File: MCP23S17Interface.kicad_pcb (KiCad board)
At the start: 2 copper layers, 55.8 x 45.4 mm, 8 parts, among them J1 Conn_01x09, J2 Conn_01x16, J3 Conn_01x03, J4 Conn_01x03, J5 Conn_01x03, U1 MCP23S17_SP

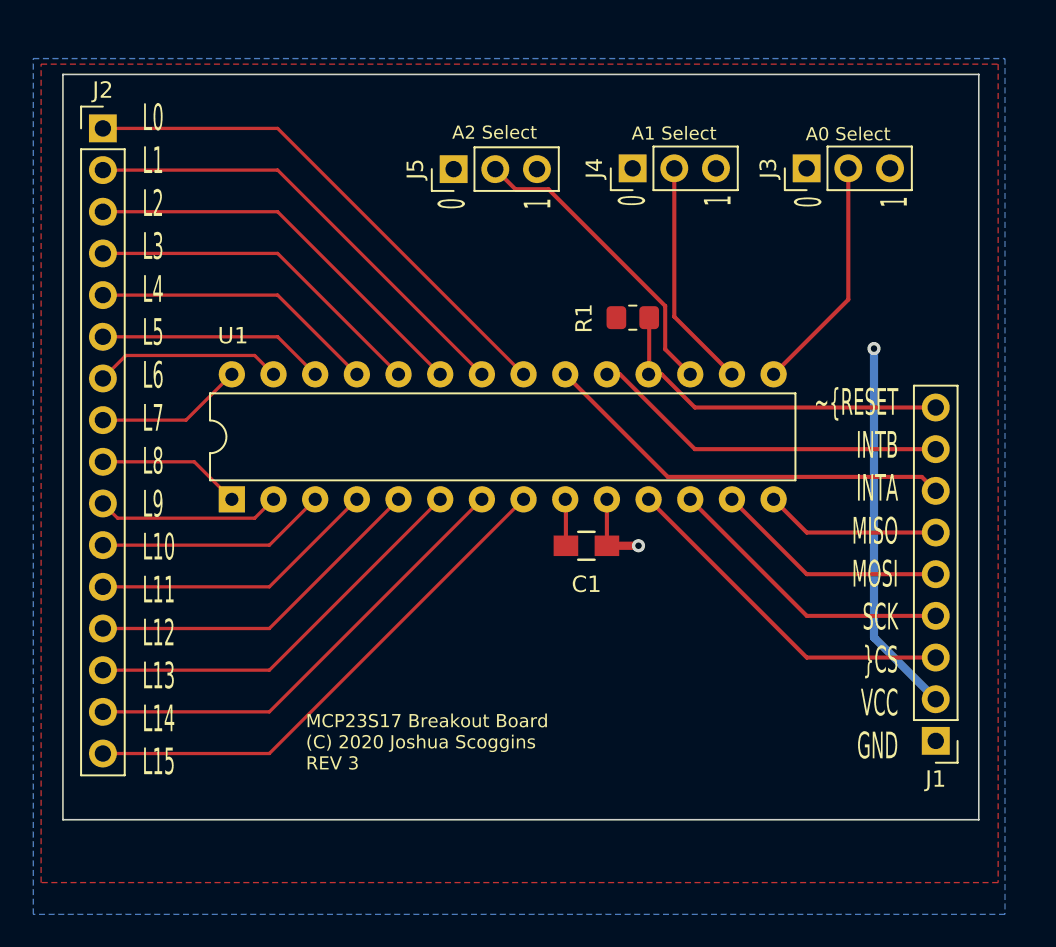
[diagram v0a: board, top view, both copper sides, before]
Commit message: Start working on the new PCB
Rearrange ordering of dip switches to make routing easier
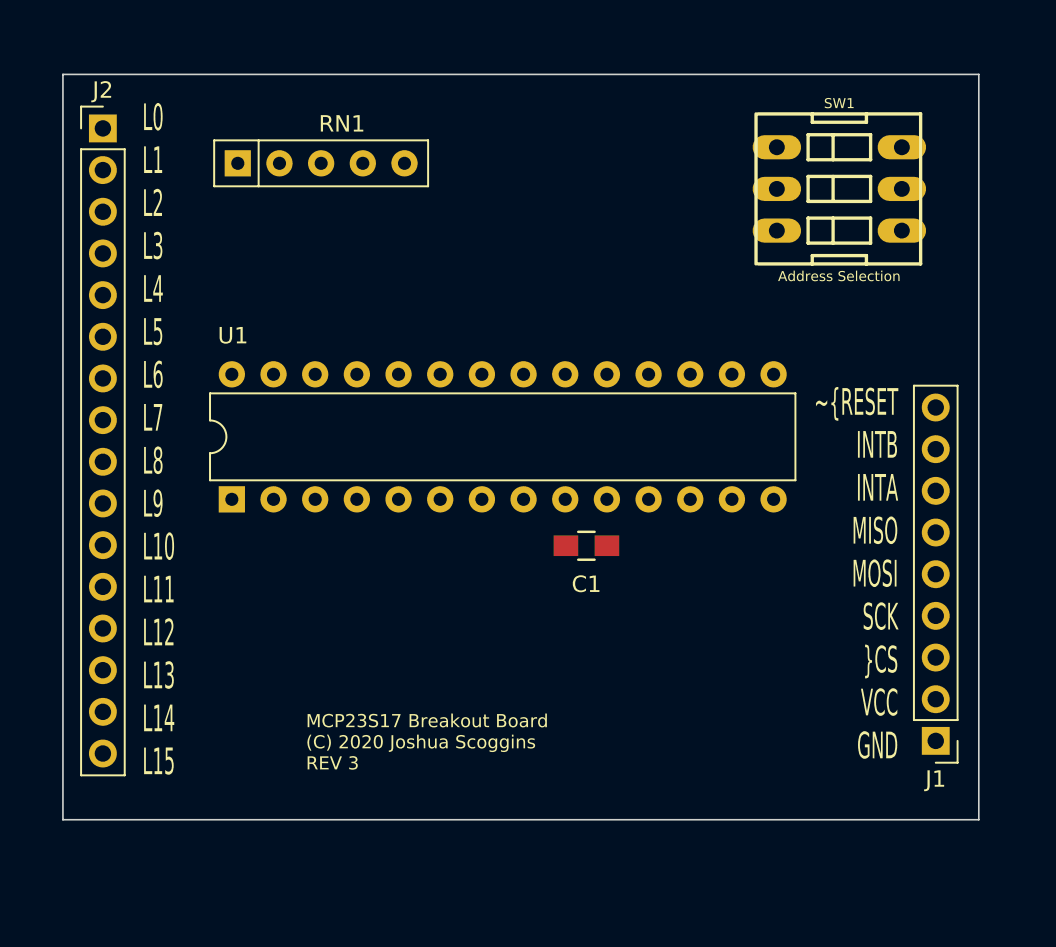
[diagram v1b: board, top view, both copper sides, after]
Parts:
- removed J3, J4, J5: Conn_01x03, Connector_PinHeader_2.54mm:PinHeader_1x03_P2.54mm_Vertical
- removed R1: 10k, Resistor_SMD:R_0805_2012Metric_Pad1.20x1.40mm_HandSolder
- added RN1: 10k, Resistor_THT:R_Array_SIP5, F.Cu at (102.7, 34.1)
- added SW1: Address Selection, Switches:DIPSWITCH-03, F.Cu at (139.3, 42.0)
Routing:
- net /L15: track 32.1 -> 0.00 mm
- net /L0: track 31.8 -> 0.00 mm
- net /L14: track 28.5 -> 0.00 mm
- net /L1: track 28.3 -> 0.00 mm
- net VCC: track 25.8 -> 0.00 mm, vias 1 -> 0
- net /INTA: track 25.5 -> 0.00 mm
- net /L13: track 24.9 -> 0.00 mm
- net /L2: track 24.7 -> 0.00 mm
- net /INTB: track 21.9 -> 0.00 mm
- net /~RESET: track 21.8 -> 0.00 mm
- net /~CS: track 21.5 -> 0.00 mm
- net /L12: track 21.3 -> 0.00 mm
- net /L3: track 21.1 -> 0.00 mm
- net /A2: track 18.6 -> 0.00 mm
- net /SCK: track 17.9 -> 0.00 mm
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- removed copper zone on B.Cu, net GND
- removed copper zone on F.Cu, net VCC
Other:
- board text removed: "0 1"
- board text removed: "A0 Select"
- board text removed: "A1 Select"
- board text removed: "A2 Select"

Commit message: Finished the rev 4 design
I have routed the resistor network directly into the trace but I'm not
sure if that is the smarter design or not. I will ponder further on this
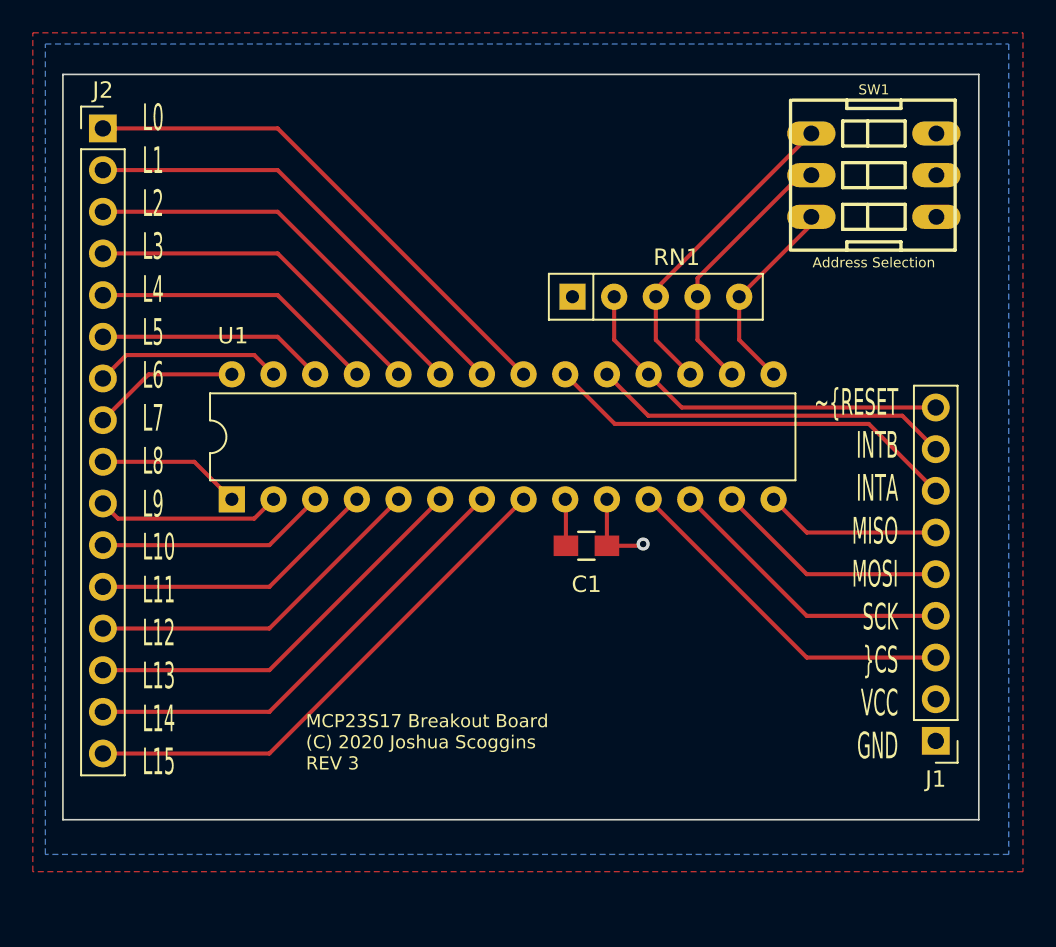
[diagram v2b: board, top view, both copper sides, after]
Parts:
- moved RN1 22.0 mm to (123.1, 42.2)
- moved SW1 2.26 mm to (141.4, 41.1)
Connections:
- RN1 pad 3: /A0 -> /A2
- RN1 pad 5: /A2 -> /A0
- SW1 pad 1: /A0 -> /A2
- SW1 pad 3: /A2 -> /A0
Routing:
- net /L15: track 0.00 -> 32.1 mm
- net /L0: track 0.00 -> 31.8 mm
- net /L14: track 0.00 -> 28.5 mm
- net /L1: track 0.00 -> 28.3 mm
- net /INTA: track 0.00 -> 25.5 mm
- net /L13: track 0.00 -> 24.9 mm
- net /L2: track 0.00 -> 24.7 mm
- net /~RESET: track 0.00 -> 23.9 mm
- net /INTB: track 0.00 -> 21.9 mm
- net /~CS: track 0.00 -> 21.5 mm
- net /L12: track 0.00 -> 21.3 mm
- net /L3: track 0.00 -> 21.1 mm
- net /A2: track 0.00 -> 19.5 mm
- net /SCK: track 0.00 -> 17.9 mm
- net /L11: track 0.00 -> 17.7 mm
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- added copper zone on B.Cu, net GND
- added copper zone on F.Cu, net VCC

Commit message: Rearrange lines further to reduce trace fanout
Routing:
- net /L15: track 32.1 -> 0.00 mm
- net /L0: track 31.8 -> 0.00 mm
- net /L14: track 28.5 -> 0.00 mm
- net /L1: track 28.3 -> 0.00 mm
- net /INTA: track 25.5 -> 0.00 mm
- net /L13: track 24.9 -> 0.00 mm
- net /L2: track 24.7 -> 0.00 mm
- net /~RESET: track 23.9 -> 0.00 mm
- net /INTB: track 21.9 -> 0.00 mm
- net /~CS: track 21.5 -> 0.00 mm
- net /L12: track 21.3 -> 0.00 mm
- net /L3: track 21.1 -> 0.00 mm
- net /A2: track 19.5 -> 0.00 mm
- net /SCK: track 17.9 -> 0.00 mm
- net /L11: track 17.7 -> 0.00 mm
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- removed copper zone on B.Cu, net GND
- removed copper zone on F.Cu, net VCC
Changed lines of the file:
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@@
     (thickness 1.6002)
     (drawings 7)
-    (tracks 72)
+    (tracks 0)
     (zones 0)
     (modules 6)
@@
     (effects (font (size 1.6256 0.8) (thickness 0.1)) (justify right))
   )
-  (via (at 127.36576 57.26938) (size 0.8) (drill 0.4) (layers Front Back) (net 1))
-  (segment (start 125.15628 57.37606) (end 127.25908 57.37606) (width 0.25) (layer Front) (net 1))
-  (segment (start 127.25908 57.37606) (end 127.36576 57.26938) (width 0.25) (layer Front) (net 1))
-  (segment (start 125.15628 54.54682) (end 125.15596 54.5465) (width 0.25) (layer Front) (net 1))
-  (segment (start 125.15628 57.37606) (end 125.15628 54.54682) (width 0.25) (layer Front) (net 1))
-  (segment (start 122.65628 54.58682) (end 122.61596 54.5465) (width 0.25) (layer Front) (net 2))
-  (segment (start 122.65628 57.37606) (end 122.65628 54.58682) (width 0.25) (layer Front) (net 2))
-  (segment (start 128.13792 41.72712) (end 137.6172 32.24784) (width 0.25) (layer Front) (net 3))
-  (segment (start 128.13792 42.19702) (end 128.13792 41.72712) (width 0.25) (layer Front) (net 3))
-  (segment (start 128.13792 44.82846) (end 130.23596 46.9265) (width 0.25) (layer Front) (net 3))
-  (segment (start 128.13792 42.19702) (end 128.13792 44.82846) (width 0.25) (layer Front) (net 3))
-  (segment (start 136.95573 34.78784) (end 137.6172 34.78784) (width 0.25) (layer Front) (net 4))
-  (segment (start 130.67792 41.06565) (end 136.95573 34.78784) (width 0.25) (layer Front) (net 4))
-  (segment (start 130.67792 42.19702) (end 130.67792 41.06565) (width 0.25) (layer Front) (net 4))
-  (segment (start 130.67792 44.82846) (end 132.77596 46.9265) (width 0.25) (layer Front) (net 4))
-  (segment (start 130.67792 42.19702) (end 130.67792 44.82846) (width 0.25) (layer Front) (net 4))
-  (segment (start 137.6172 37.79774) (end 137.6172 37.32784) (width 0.25) (layer Front) (net 5))
-  (segment (start 133.21792 42.19702) (end 137.6172 37.79774) (width 0.25) (layer Front) (net 5))
-  (segment (start 133.21792 44.82846) (end 135.31596 46.9265) (width 0.25) (layer Front) (net 5))
-  (segment (start 133.21792 42.19702) (end 133.21792 44.82846) (width 0.25) (layer Front) (net 5))
-  (segment (start 145.1991 51.48834) (end 143.15911 49.44835) (width 0.25) (layer Front) (net 6))
-  (segment (start 143.15911 49.44835) (end 127.67781 49.44835) (width 0.25) (layer Front) (net 6))
-  (segment (start 127.67781 49.44835) (end 125.15596 46.9265) (width 0.25) (layer Front) (net 6))
-  (segment (start 141.119121 49.948361) (end 145.1991 54.02834) (width 0.25) (layer Front) (net 7))
-  (segment (start 125.637821 49.948361) (end 141.119121 49.948361) (width 0.25) (layer Front) (net 7))
-  (segment (start 122.61596 46.9265) (end 125.637821 49.948361) (width 0.25) (layer Front) (net 7))
-  (segment (start 125.59792 44.82846) (end 127.69596 46.9265) (width 0.25) (layer Front) (net 8))
-  (segment (start 125.59792 42.19702) (end 125.59792 44.82846) (width 0.25) (layer Front) (net 8))
-  (segment (start 129.7178 48.94834) (end 127.69596 46.9265) (width 0.25) (layer Front) (net 8))
-  (segment (start 145.1991 48.94834) (end 129.7178 48.94834) (width 0.25) (layer Front) (net 8))
-  (segment (start 137.3378 56.56834) (end 135.31596 54.5465) (width 0.25) (layer Front) (net 9))
-  (segment (start 145.1991 56.56834) (end 137.3378 56.56834) (width 0.25) (layer Front) (net 9))
-  (segment (start 137.3378 59.10834) (end 145.1991 59.10834) (width 0.25) (layer Front) (net 10))
-  (segment (start 132.77596 54.5465) (end 137.3378 59.10834) (width 0.25) (layer Front) (net 10))
-  (segment (start 137.3378 61.64834) (end 130.23596 54.5465) (width 0.25) (layer Front) (net 11))
-  (segment (start 145.1991 61.64834) (end 137.3378 61.64834) (width 0.25) (layer Front) (net 11))
-  (segment (start 137.3378 64.18834) (end 145.1991 64.18834) (width 0.25) (layer Front) (net 12))
-  (segment (start 127.69596 54.5465) (end 137.3378 64.18834) (width 0.25) (layer Front) (net 12))
-  (segment (start 104.5845 70.03796) (end 120.07596 54.5465) (width 0.25) (layer Front) (net 13))
-  (segment (start 94.4372 70.03796) (end 104.5845 70.03796) (width 0.25) (layer Front) (net 13))
-  (segment (start 104.5845 67.49796) (end 117.53596 54.5465) (width 0.25) (layer Front) (net 14))
-  (segment (start 94.4372 67.49796) (end 104.5845 67.49796) (width 0.25) (layer Front) (net 14))
-  (segment (start 104.5845 64.95796) (end 114.99596 54.5465) (width 0.25) (layer Front) (net 15))
-  (segment (start 94.4372 64.95796) (end 104.5845 64.95796) (width 0.25) (layer Front) (net 15))
-  (segment (start 104.5845 62.41796) (end 112.45596 54.5465) (width 0.25) (layer Front) (net 16))
-  (segment (start 94.4372 62.41796) (end 104.5845 62.41796) (width 0.25) (layer Front) (net 16))
-  (segment (start 104.5845 59.87796) (end 109.91596 54.5465) (width 0.25) (layer Front) (net 17))
-  (segment (start 94.4372 59.87796) (end 104.5845 59.87796) (width 0.25) (layer Front) (net 17))
-  (segment (start 104.5845 57.33796) (end 107.37596 54.5465) (width 0.25) (layer Front) (net 18))
-  (segment (start 94.4372 57.33796) (end 104.5845 57.33796) (width 0.25) (layer Front) (net 18))
-  (segment (start 103.660959 55.721501) (end 104.83596 54.5465) (width 0.25) (layer Front) (net 19))
-  (segment (start 95.360741 55.721501) (end 103.660959 55.721501) (width 0.25) (layer Front) (net 19))
-  (segment (start 94.4372 54.79796) (end 95.360741 55.721501) (width 0.25) (layer Front) (net 19))
-  (segment (start 100.00742 52.25796) (end 102.29596 54.5465) (width 0.25) (layer Front) (net 20))
-  (segment (start 94.4372 52.25796) (end 100.00742 52.25796) (width 0.25) (layer Front) (net 20))
-  (segment (start 97.22866 46.9265) (end 94.4372 49.71796) (width 0.25) (layer Front) (net 21))
-  (segment (start 102.29596 46.9265) (end 97.22866 46.9265) (width 0.25) (layer Front) (net 21))
-  (segment (start 95.863661 45.751499) (end 94.4372 47.17796) (width 0.25) (layer Front) (net 22))
-  (segment (start 103.660959 45.751499) (end 95.863661 45.751499) (width 0.25) (layer Front) (net 22))
-  (segment (start 104.83596 46.9265) (end 103.660959 45.751499) (width 0.25) (layer Front) (net 22))
-  (segment (start 105.08742 44.63796) (end 94.4372 44.63796) (width 0.25) (layer Front) (net 23))
-  (segment (start 107.37596 46.9265) (end 105.08742 44.63796) (width 0.25) (layer Front) (net 23))
-  (segment (start 105.08742 42.09796) (end 94.4372 42.09796) (width 0.25) (layer Front) (net 24))
-  (segment (start 109.91596 46.9265) (end 105.08742 42.09796) (width 0.25) (layer Front) (net 24))
-  (segment (start 105.08742 39.55796) (end 94.4372 39.55796) (width 0.25) (layer Front) (net 25))
-  (segment (start 112.45596 46.9265) (end 105.08742 39.55796) (width 0.25) (layer Front) (net 25))
-  (segment (start 105.08742 37.01796) (end 114.99596 46.9265) (width 0.25) (layer Front) (net 26))
-  (segment (start 94.4372 37.01796) (end 105.08742 37.01796) (width 0.25) (layer Front) (net 26))
-  (segment (start 105.08742 34.47796) (end 117.53596 46.9265) (width 0.25) (layer Front) (net 27))
-  (segment (start 94.4372 34.47796) (end 105.08742 34.47796) (width 0.25) (layer Front) (net 27))
-  (segment (start 105.08742 31.93796) (end 94.4372 31.93796) (width 0.25) (layer Front) (net 28))
-  (segment (start 120.07596 46.9265) (end 105.08742 31.93796) (width 0.25) (layer Front) (net 28))
   (zone (net 0) (net_name "") (layers F&B.Cu) (hatch edge 0.508)
     (connect_pads (clearance 0.508))
@@
       )
     )
-  )
-  (zone (net 2) (net_name VCC) (layer Front) (hatch edge 0.508)
-    (connect_pads (clearance 0.508))
-    (min_thickness 0.254)
-    (fill yes (arc_segments 32) (thermal_gap 0.508) (thermal_bridge_width 0.508))
-    (polygon
-      (pts
-        (xy 150.51532 77.23886) (xy 90.16492 77.23886) (xy 90.16492 26.1112) (xy 150.51532 26.1112)
-      )
-    )
-  )
-  (zone (net 1) (net_name GND) (layer Back) (hatch edge 0.508)
-    (connect_pads (clearance 0.508))
-    (min_thickness 0.254)
-    (fill yes (arc_segments 32) (thermal_gap 0.508) (thermal_bridge_width 0.508))
-    (polygon
-      (pts
-        (xy 149.64918 76.1873) (xy 90.92946 76.1873) (xy 90.92946 26.79446) (xy 149.64918 26.79446)
-      )
-    )
